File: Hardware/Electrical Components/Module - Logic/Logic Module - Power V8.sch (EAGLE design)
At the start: 23 parts, among them Q2 130mA/20V

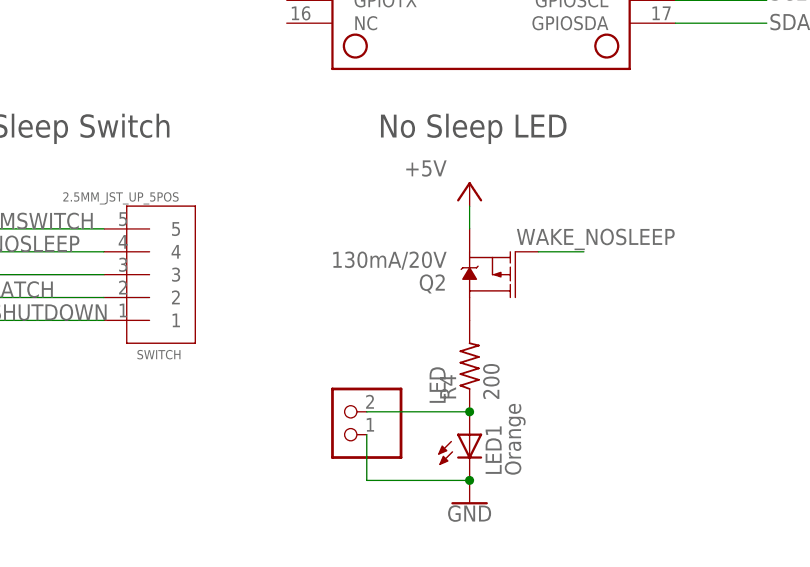
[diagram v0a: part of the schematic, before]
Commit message: Clarify text in PCBs
O Add text for 3PDT Switch breakout board better PCB annotation
O Rename MOSFET that controls LED for Programming Mode -> P_MOS
+ Add JST Male to BOM Logic Module – Power V8
O Correct excel formula for a total price of Logic Module
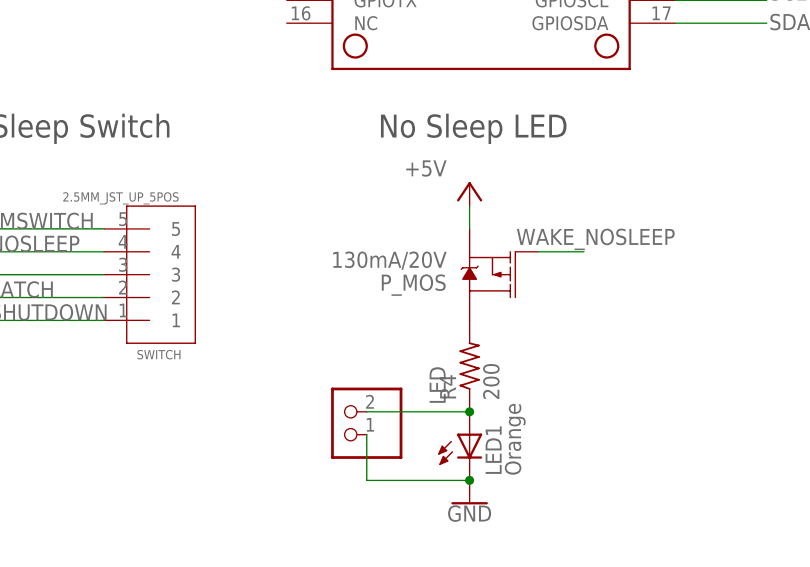
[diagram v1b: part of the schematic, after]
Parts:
- renumbered Q2 to P_MOS
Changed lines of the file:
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@@
 <part name="LED1" library="adafruit" library_urn="urn:adsk.eagle:library:420" deviceset="LED" device="3MM" package3d_urn="urn:adsk.eagle:package:6240537/1" value="Orange"/>
 <part name="GND2" library="SparkFun-PowerSymbols" library_urn="urn:adsk.eagle:library:530" deviceset="GND" device=""/>
-<part name="Q2" library="SparkFun-DiscreteSemi" library_urn="urn:adsk.eagle:library:514" deviceset="MOSFET_PCH" device="-IRLML2244" package3d_urn="urn:adsk.eagle:package:38446/1" value="130mA/20V"/>
+<part name="P_MOS" library="SparkFun-DiscreteSemi" library_urn="urn:adsk.eagle:library:514" deviceset="MOSFET_PCH" device="-IRLML2244" package3d_urn="urn:adsk.eagle:package:38446/1" value="130mA/20V"/>
 <part name="LED" library="eDNA" deviceset="2.5MM_JST_UP_2POS" device=""/>
 <part name="MS1" library="adafruit" deviceset="FEATHERWING" device="" package3d_urn="urn:adsk.eagle:package:6240959/1"/>
@@
 <attribute name="VALUE" x="-5.08" y="-40.894" size="1.778" layer="96" align="top-center"/>
 </instance>
-<instance part="Q2" gate="G$1" x="-2.54" y="-15.24" smashed="yes" rot="R180">
+<instance part="P_MOS" gate="G$1" x="-2.54" y="-15.24" smashed="yes" rot="R180">
 <attribute name="NAME" x="-7.62" y="-15.24" size="1.778" layer="95" font="vector" rot="R180"/>
 <attribute name="VALUE" x="-7.62" y="-12.7" size="1.778" layer="96" font="vector" rot="R180"/>
@@
 </segment>
 <segment>
-<pinref part="Q2" gate="G$1" pin="S"/>
+<pinref part="P_MOS" gate="G$1" pin="S"/>
 <wire x1="-5.08" y1="-7.62" x2="-5.08" y2="-10.16" width="0.1524" layer="91"/>
 <pinref part="P+4" gate="1" pin="+5V"/>
@@
 <wire x1="2.54" y1="-12.7" x2="7.62" y2="-12.7" width="0.1524" layer="91"/>
 <label x="17.78" y="-10.16" size="1.778" layer="95" rot="R180"/>
-<pinref part="Q2" gate="G$1" pin="G"/>
+<pinref part="P_MOS" gate="G$1" pin="G"/>
 </segment>
 <segment>
@@
 <net name="N$2" class="0">
 <segment>
-<pinref part="Q2" gate="G$1" pin="D"/>
+<pinref part="P_MOS" gate="G$1" pin="D"/>
 <pinref part="R4" gate="G$1" pin="2"/>
 </segment>
